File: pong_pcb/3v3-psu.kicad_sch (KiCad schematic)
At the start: 10 parts, among them IC1 MAX17626ATA+T

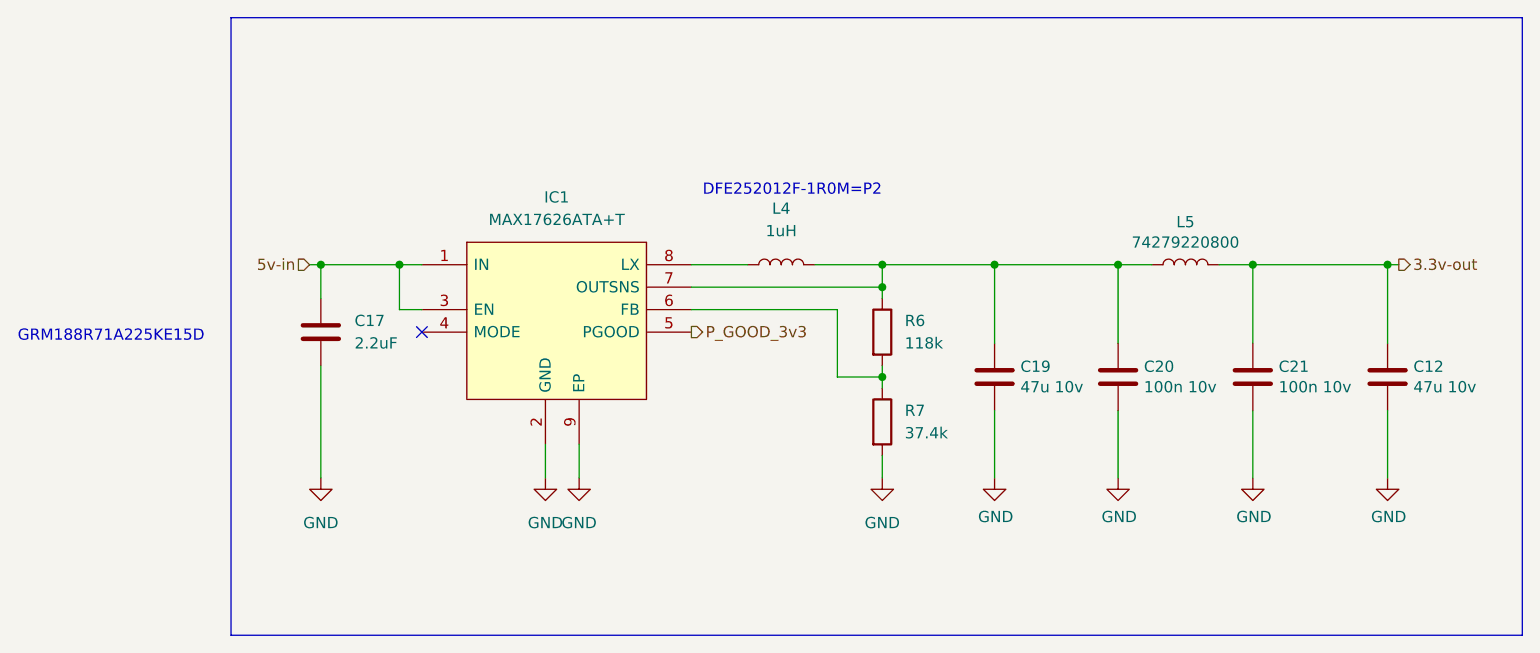
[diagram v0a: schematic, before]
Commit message: Update schema and add packages
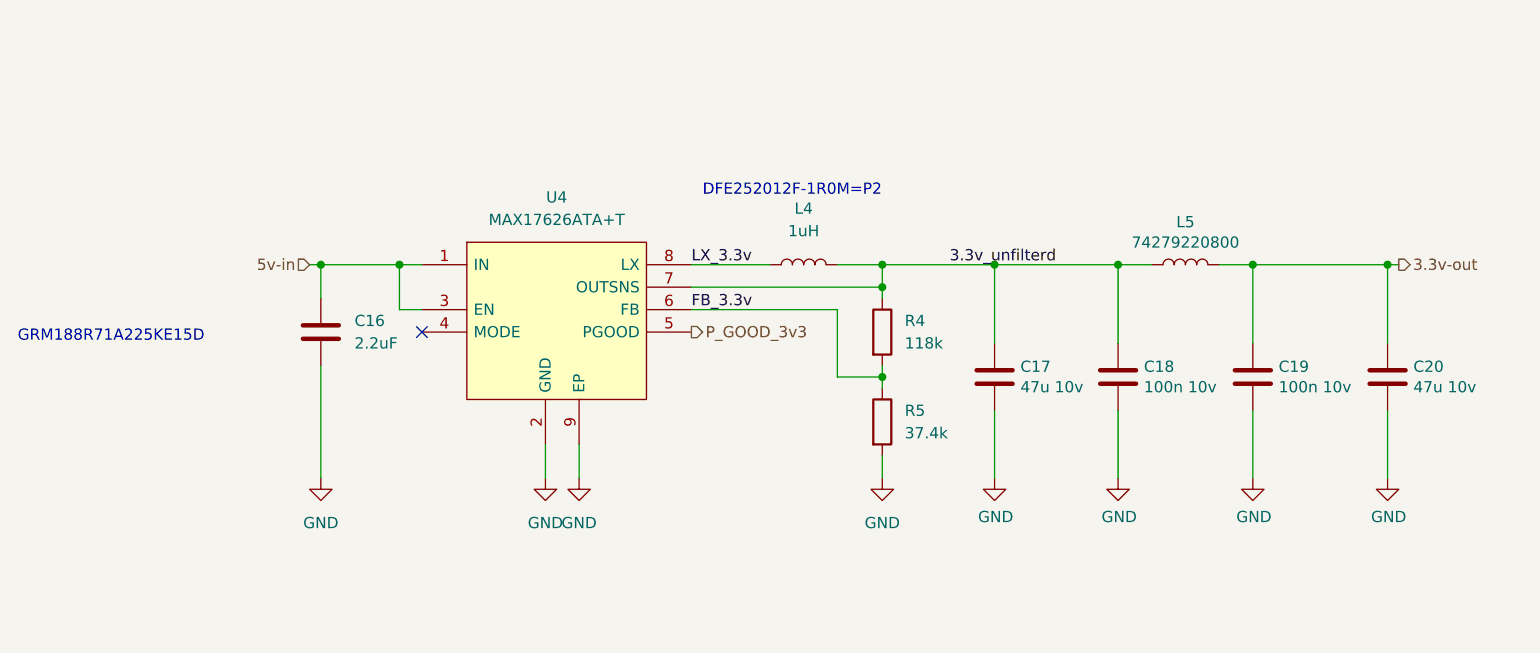
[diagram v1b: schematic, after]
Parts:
- removed IC1: MAX17626ATA+T, MyLib:SON50P200X200X80-9N-D, symbol myLib:MAX17626ATA+T
- added U4: MAX17626ATA+T, MyLib:SON50P200X200X80-9N-D, symbol MyLib:MAX17626ATA+T
- C17: renamed from C19; footprint Capacitor_SMD:C_1206_3216Metric_Pad1.42x1.75mm_HandSolder -> Capacitor_SMD:C_1206_3216Metric_Pad1.33x1.80mm_HandSolder
- C20: renamed from C12; footprint Capacitor_SMD:C_1206_3216Metric_Pad1.42x1.75mm_HandSolder -> Capacitor_SMD:C_1206_3216Metric_Pad1.33x1.80mm_HandSolder
- renumbered C17 to C16, C20 to C18, C21 to C19, R6 to R4, R7 to R5
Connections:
- net 5v-in: now also U4.1 (IN), U4.3 (EN)
- net GND: now also U4.2 (GND), U4.9 (EP)
- net P_GOOD_3v3: now also U4.5 (PGOOD)
- net 3.3v_unfilterd: now reaches C17.1, C18.1, L4.2, L5.1, R4.1
- net 3.3v_unfilterd: now also U4.7 (OUTSNS)
- net FB_3.3v: now reaches R4.2, R5.1
- net FB_3.3v: now also U4.6 (FB)
- net LX_3.3v: now reaches L4.1
- net LX_3.3v: now also U4.8 (LX)
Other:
- company: (none) -> Fontys
- title: (none) -> 3.3V power supply
- moved on the sheet: L4

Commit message: Add HDMI layout
And others
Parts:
- C18, C19: footprint Capacitor_SMD:C_0402_1005Metric_Pad0.74x0.62mm_HandSolder -> Capacitor_SMD:C_0603_1608Metric
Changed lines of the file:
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@@
 			)
 		)
-		(property "Footprint" "Capacitor_SMD:C_0402_1005Metric_Pad0.74x0.62mm_HandSolder"
+		(property "Footprint" "Capacitor_SMD:C_0603_1608Metric"
 			(at 182.5752 104.14 0)
 			(effects
@@
 			)
 		)
-		(property "Footprint" "Capacitor_SMD:C_0402_1005Metric_Pad0.74x0.62mm_HandSolder"
+		(property "Footprint" "Capacitor_SMD:C_0603_1608Metric"
 			(at 197.8152 104.14 0)
 			(effects

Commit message: Update schema and route PCB
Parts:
- renumbered C16 to C17, C17 to C18, C18 to C19, C19 to C20, C20 to C21
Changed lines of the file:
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@@
 		(on_board yes)
 		(dnp no)
-		(property "Reference" "#PWR037"
+		(property "Reference" "#PWR042"
 			(at 167.64 118.11 0)
 			(effects
@@
 			(project "pong_pcb"
 				(path "/676c80a8-0f91-4e34-b1e8-b545e51bb5da/00c898c2-6b95-43d5-ade7-f24f2a0af2a5"
-					(reference "#PWR037")
+					(reference "#PWR042")
 					(unit 1)
 				)
@@
 		(dnp no)
 		(fields_autoplaced yes)
-		(property "Reference" "#PWR033"
+		(property "Reference" "#PWR038"
 			(at 91.44 118.11 0)
 			(effects
@@
 			(project "pong_pcb"
 				(path "/676c80a8-0f91-4e34-b1e8-b545e51bb5da/00c898c2-6b95-43d5-ade7-f24f2a0af2a5"
-					(reference "#PWR033")
+					(reference "#PWR038")
 					(unit 1)
 				)
@@
 		(dnp no)
 		(fields_autoplaced yes)
-		(property "Reference" "#PWR034"
+		(property "Reference" "#PWR039"
 			(at 116.84 118.11 0)
 			(effects
@@
 			(project "pong_pcb"
 				(path "/676c80a8-0f91-4e34-b1e8-b545e51bb5da/00c898c2-6b95-43d5-ade7-f24f2a0af2a5"
-					(reference "#PWR034")
+					(reference "#PWR039")
 					(unit 1)
 				)
@@
 		(on_board yes)
 		(dnp no)
-		(property "Reference" "#PWR038"
+		(property "Reference" "#PWR043"
 			(at 181.61 118.11 0)
 			(effects
@@
 			(project "pong_pcb"
 				(path "/676c80a8-0f91-4e34-b1e8-b545e51bb5da/00c898c2-6b95-43d5-ade7-f24f2a0af2a5"
-					(reference "#PWR038")
+					(reference "#PWR043")
 					(unit 1)
 				)
@@
 		(on_board yes)
 		(dnp no)
-		(property "Reference" "#PWR039"
+		(property "Reference" "#PWR044"
 			(at 196.85 118.11 0)
 			(effects
@@
 			(project "pong_pcb"
 				(path "/676c80a8-0f91-4e34-b1e8-b545e51bb5da/00c898c2-6b95-43d5-ade7-f24f2a0af2a5"
-					(reference "#PWR039")
+					(reference "#PWR044")
 					(unit 1)
 				)
@@
 		(dnp no)
 		(fields_autoplaced yes)
-		(property "Reference" "#PWR035"
+		(property "Reference" "#PWR040"
 			(at 120.65 118.11 0)
 			(effects
@@
 			(project "pong_pcb"
 				(path "/676c80a8-0f91-4e34-b1e8-b545e51bb5da/00c898c2-6b95-43d5-ade7-f24f2a0af2a5"
-					(reference "#PWR035")
+					(reference "#PWR040")
 					(unit 1)
 				)
@@
 		(on_board yes)
 		(dnp no)
-		(property "Reference" "C16"
+		(property "Reference" "C17"
 			(at 95.25 93.9799 0)
 			(effects
@@
 			(project "pong_pcb"
 				(path "/676c80a8-0f91-4e34-b1e8-b545e51bb5da/00c898c2-6b95-43d5-ade7-f24f2a0af2a5"
-					(reference "C16")
+					(reference "C17")
 					(unit 1)
 				)
@@
 		(dnp no)
 		(fields_autoplaced yes)
-		(property "Reference" "#PWR036"
+		(property "Reference" "#PWR041"
 			(at 154.94 118.11 0)
 			(effects
@@
 			(project "pong_pcb"
 				(path "/676c80a8-0f91-4e34-b1e8-b545e51bb5da/00c898c2-6b95-43d5-ade7-f24f2a0af2a5"
-					(reference "#PWR036")
+					(reference "#PWR041")
 					(unit 1)
 				)
@@
 		(on_board yes)
 		(dnp no)
-		(property "Reference" "C20"
+		(property "Reference" "C21"
 			(at 215.011 99.1616 0)
 			(effects
@@
 			(project "pong_pcb"
 				(path "/676c80a8-0f91-4e34-b1e8-b545e51bb5da/00c898c2-6b95-43d5-ade7-f24f2a0af2a5"
-					(reference "C20")
+					(reference "C21")
 					(unit 1)
 				)
@@
 		(on_board yes)
 		(dnp no)
-		(property "Reference" "C17"
+		(property "Reference" "C18"
 			(at 170.561 99.1616 0)
 			(effects
@@
 			(project "pong_pcb"
 				(path "/676c80a8-0f91-4e34-b1e8-b545e51bb5da/00c898c2-6b95-43d5-ade7-f24f2a0af2a5"
-					(reference "C17")
+					(reference "C18")
 					(unit 1)
 				)
@@
 		(on_board yes)
 		(dnp no)
-		(property "Reference" "C18"
+		(property "Reference" "C19"
 			(at 184.531 99.1616 0)
 			(effects
@@
 			(project "pong_pcb"
 				(path "/676c80a8-0f91-4e34-b1e8-b545e51bb5da/00c898c2-6b95-43d5-ade7-f24f2a0af2a5"
-					(reference "C18")
+					(reference "C19")
 					(unit 1)
 				)
@@
 		(on_board yes)
 		(dnp no)
-		(property "Reference" "C19"
+		(property "Reference" "C20"
 			(at 199.771 99.1616 0)
 			(effects
@@
 			(project "pong_pcb"
 				(path "/676c80a8-0f91-4e34-b1e8-b545e51bb5da/00c898c2-6b95-43d5-ade7-f24f2a0af2a5"
-					(reference "C19")
+					(reference "C20")
 					(unit 1)
 				)
@@
 		(on_board yes)
 		(dnp no)
-		(property "Reference" "#PWR040"
+		(property "Reference" "#PWR045"
 			(at 212.09 118.11 0)
 			(effects
@@
 			(project "pong_pcb"
 				(path "/676c80a8-0f91-4e34-b1e8-b545e51bb5da/00c898c2-6b95-43d5-ade7-f24f2a0af2a5"
-					(reference "#PWR040")
-					(unit 1)
-				)
+					(reference "#PWR045")
+					(unit 1)
+				)

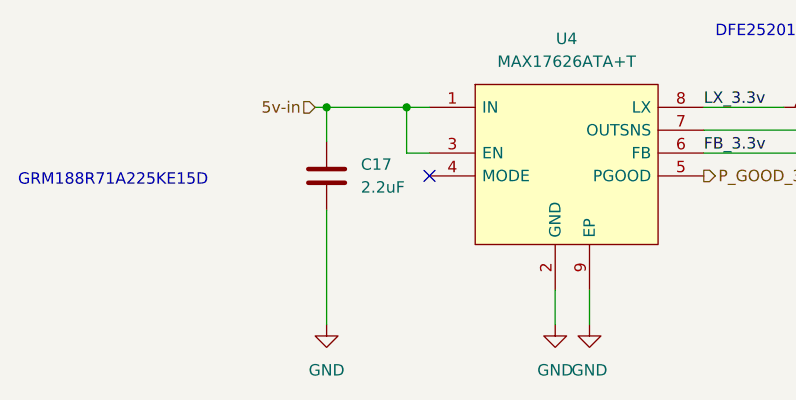
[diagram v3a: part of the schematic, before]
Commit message: Fix HDMI pinout
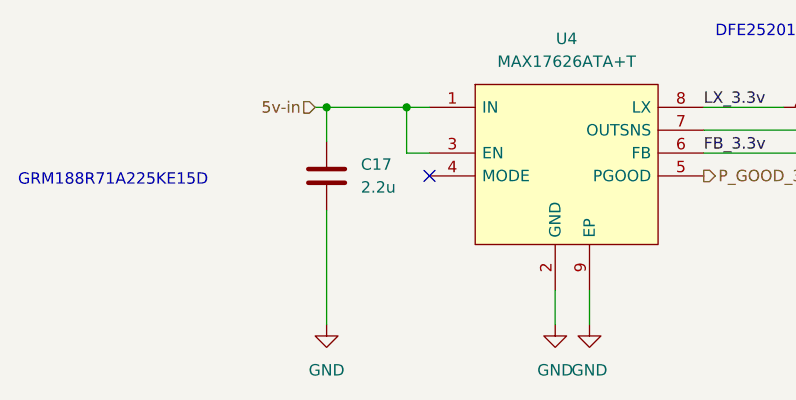
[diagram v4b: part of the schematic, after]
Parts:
- C17: value 2.2uF -> 2.2u
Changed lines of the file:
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@@
 			)
 		)
-		(property "Value" "2.2uF"
+		(property "Value" "2.2u"
 			(at 95.25 96.52 0)
 			(effects
